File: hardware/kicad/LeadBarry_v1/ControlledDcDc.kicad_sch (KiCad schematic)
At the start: 7 parts, among them Q5 2N7002, U4 XL6019E1 Module

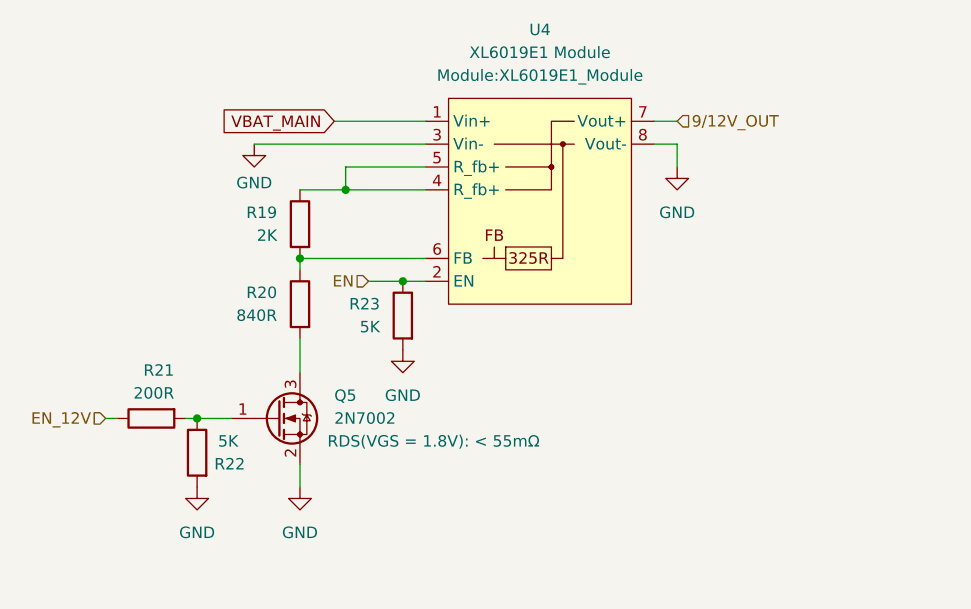
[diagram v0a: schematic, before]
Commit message: fix: pwm-controlled dc-dc output voltage
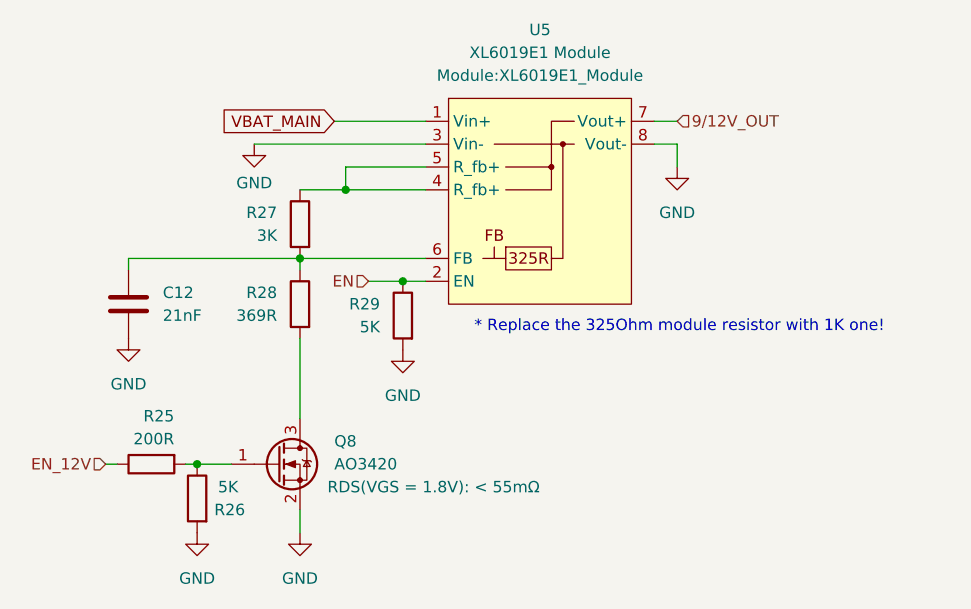
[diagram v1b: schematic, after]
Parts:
- added C12: 21nF, symbol Device:C
- Q8: renamed from Q5; value 2N7002 -> AO3420
- R27: renamed from R19; value 2K -> 3K
- R28: renamed from R20; value 840R -> 369R
- renumbered R21 to R25, R22 to R26, R23 to R29, U4 to U5
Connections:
- net GND: now also C12.2
- net at R27.2, R28.1, U5.6 (FB): now also C12.1
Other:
- note added: "* Replace the 325Ohm module resistor with 1K one!"
- moved on the sheet: Q8, R25, R26

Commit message: Revert "fix: pwm-controlled dc-dc output voltage"
This reverts commit b0b1c2266e3c7e9cf1a5c295a0eb9d631b1ef3e0.
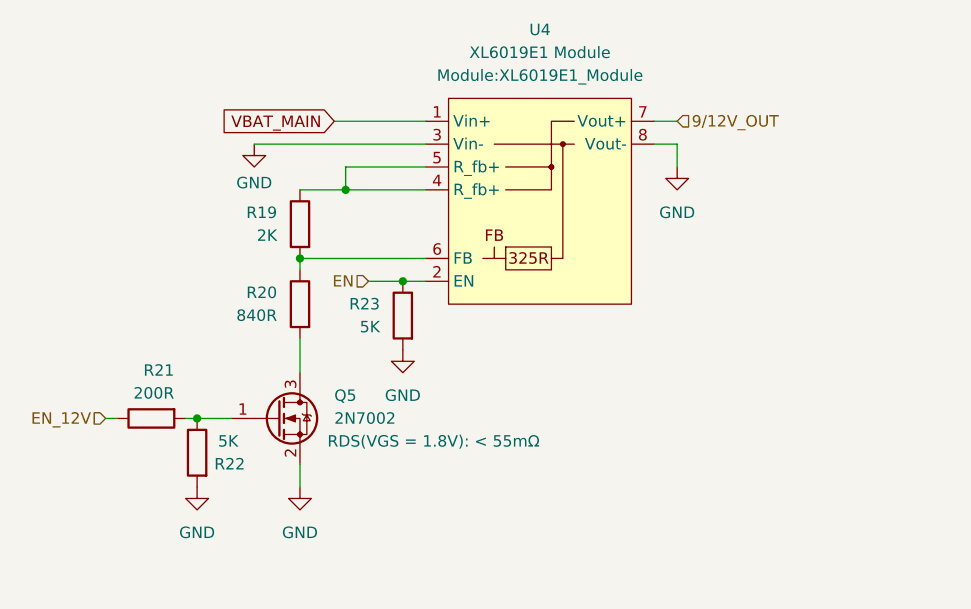
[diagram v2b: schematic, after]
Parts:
- removed C12: 21nF, symbol Device:C
- Q5: renamed from Q8; value AO3420 -> 2N7002
- R19: renamed from R27; value 3K -> 2K
- R20: renamed from R28; value 369R -> 840R
- renumbered R25 to R21, R26 to R22, R29 to R23, U5 to U4
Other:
- note removed: "* Replace the 325Ohm module resistor with 1K one!"
- moved on the sheet: Q5, R21, R22
